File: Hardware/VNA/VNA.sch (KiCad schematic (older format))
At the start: 28 parts, among them J1 USB_B_Micro, J2 USB_A, J3 Conn_ARM_SWD, J4 SMA, J5 SMA, J6 UART, U1 TPD2S017, U2 TPD2S017

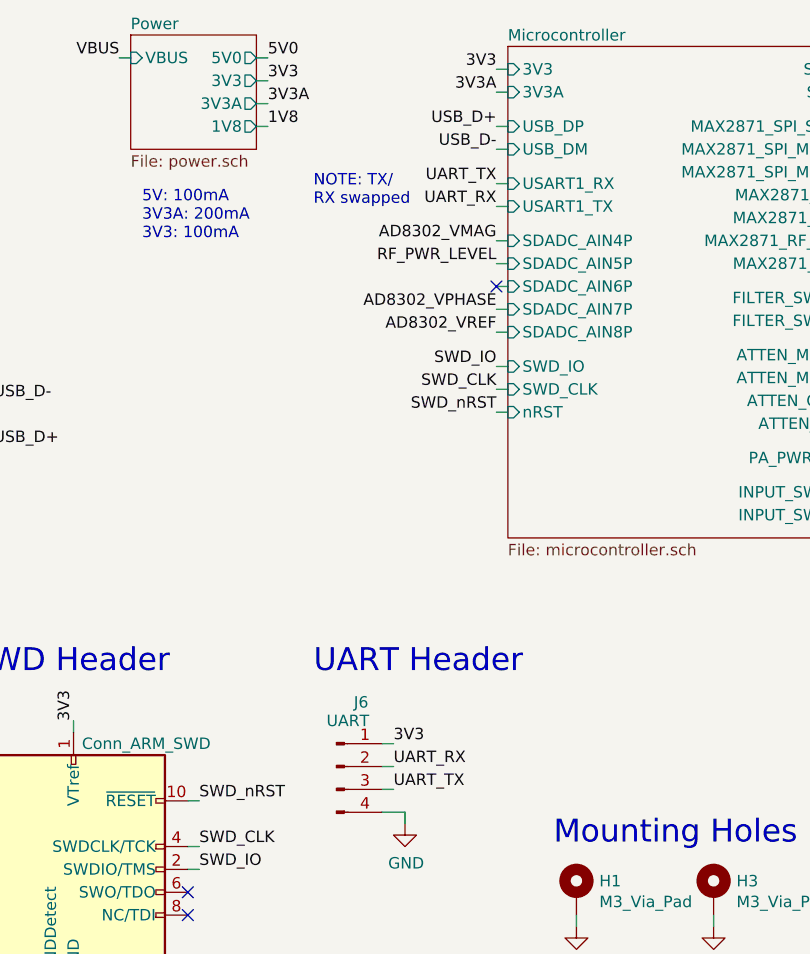
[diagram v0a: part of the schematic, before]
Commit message: FW for V0 init, functinal diagram / schematic updated freq ranges
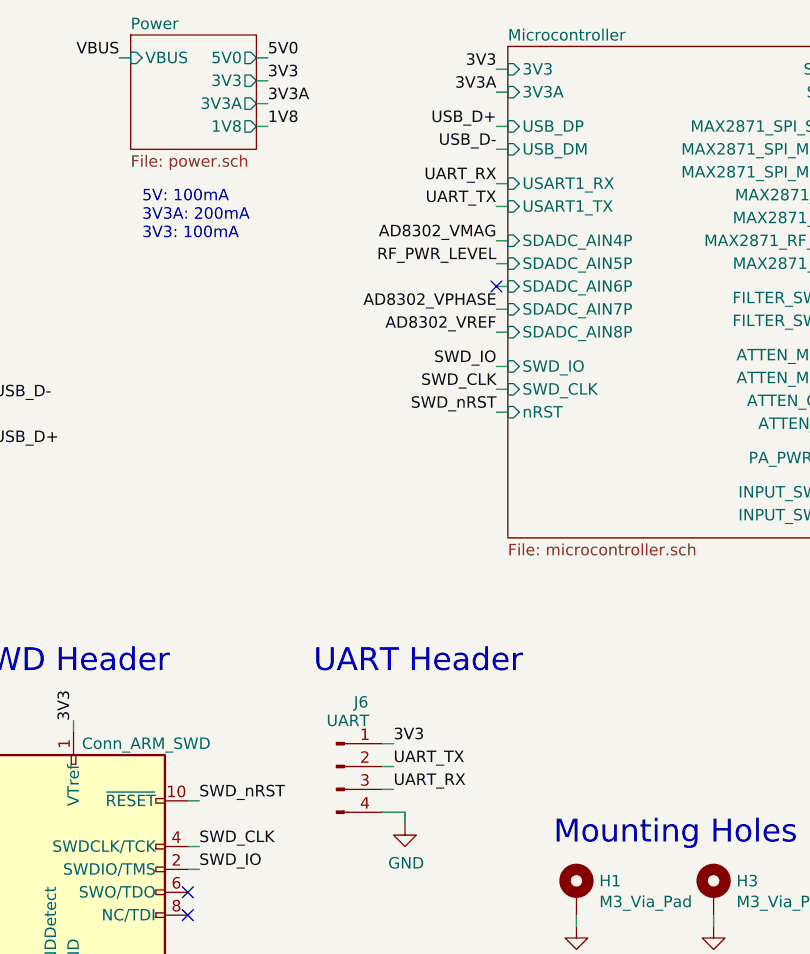
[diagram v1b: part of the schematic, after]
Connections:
- net UART_RX: now also J6.3 (Pin_3); no longer J6.2 (Pin_2)
- net UART_TX: now also J6.2 (Pin_2); no longer J6.3 (Pin_3)
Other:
- note removed: "NOTE: TX/\nRX swapped"
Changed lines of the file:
@@
 Text Notes 4450 5900 0    100  ~ 0
 UART Header
+Text Label 5250 3850 2    50   ~ 0
+UART_TX
 Text Label 5250 3750 2    50   ~ 0
+UART_RX
+Text Label 4800 6300 0    50   ~ 0
 UART_TX
-Text Label 5250 3850 2    50   ~ 0
-UART_RX
 Text Label 4800 6400 0    50   ~ 0
-UART_TX
-Text Label 4800 6300 0    50   ~ 0
 UART_RX
 Wire Wire Line
@@
 Wire Wire Line
 	1450 6900 1150 6900
-Text Notes 4450 3850 0    50   ~ 0
-NOTE: TX/\nRX swapped
 $EndSCHEMATC
